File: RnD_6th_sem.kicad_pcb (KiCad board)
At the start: 2 copper layers, 62 x 69.1 mm, 79 parts, among them IC1 2EDF7275KXUMA1, J1 HVDC, J10 MMCX-J-P-H-ST-TH1, J2 PWM, J3 HVDC, J4 Conn_02x05_Odd_Even, J5 5V, J6 5V, J7 GND, J8 GND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

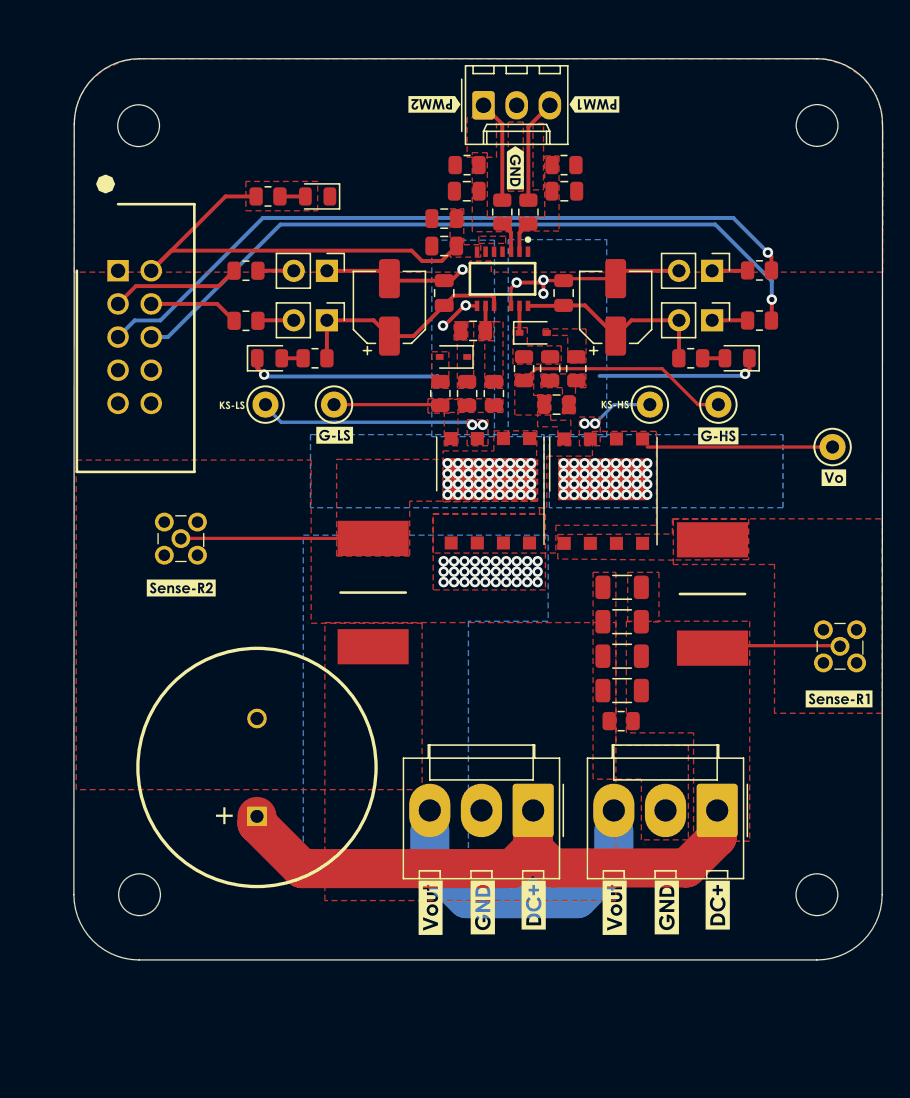
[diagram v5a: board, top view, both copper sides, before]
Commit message: updated the layout of FB and caps
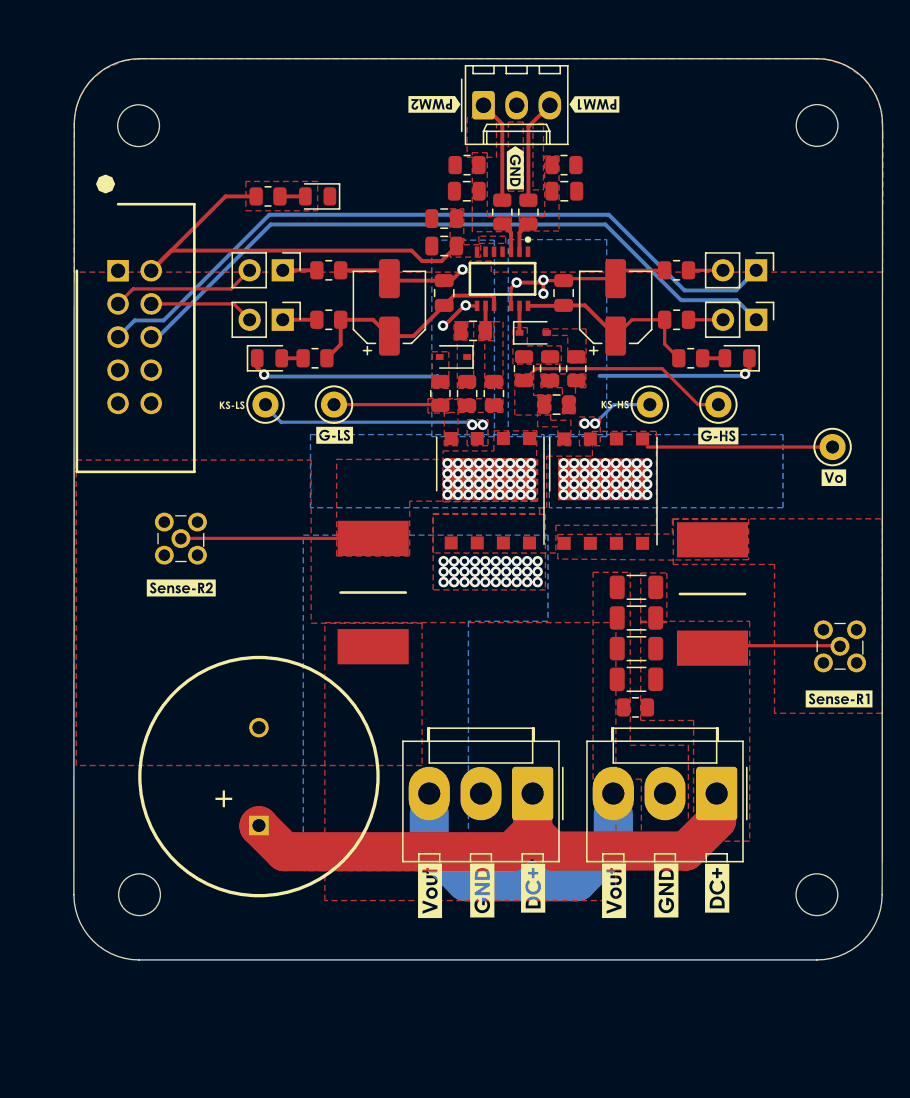
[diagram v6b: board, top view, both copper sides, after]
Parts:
- added kibuzzard-63FF27E9: G***, kibuzzard-63FF27E9, B.Cu at (153.1, 96.2)
- added kibuzzard-63FF2952: G***, kibuzzard-63FF2952, B.Cu at (124.6, 77.9)
- moved FB4 6.35 mm to (152.0, 67.8), turned to 0 degrees
- moved FB1 6.35 mm to (152.0, 64.0)
- moved FB3 6.34 mm to (125.4, 67.8), turned to 180 degrees
- moved FB2 6.34 mm to (125.4, 64.0)
- moved J6 3.38 mm to (121.9, 67.8)
- moved J7 3.38 mm to (121.9, 64.0)
- moved J5 3.38 mm to (158.1, 67.8)
- moved J8 3.38 mm to (158.1, 64.0)
- moved R8 1.52 mm to (148.9, 97.5)
- moved C7 1.40 mm to (149.0, 95.3)
- moved kibuzzard-63EE9044 1.30 mm to (155.1, 111.3)
- moved kibuzzard-63EE9044 1.30 mm to (141.0, 111.3)
- moved kibuzzard-63EE9059 1.30 mm to (137.1, 111.5)
- moved kibuzzard-63EE9091 1.30 mm to (133.1, 111.5)
- moved J1 1.30 mm to (155.1, 104.1)
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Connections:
- FB1 pad 1: GND1 -> gnd-1
- FB2 pad 2: GND2 -> gnd-2
- FB3 pad 1: Net-(FB3-Pad1) -> LED2
- FB3 pad 2: VCCB -> Net-(FB3-Pad2)
- FB4 pad 1: Net-(FB4-Pad1) -> LED1
- FB4 pad 2: VCCA -> Net-(FB4-Pad2)
- J4 pad 3: Net-(FB2-Pad1) -> GND2
- J4 pad 4: Net-(FB3-Pad1) -> VCCB
- J4 pad 5: Net-(FB1-Pad2) -> GND1
- J4 pad 6: Net-(FB4-Pad1) -> VCCA
- J5 pad 2: LED1 -> Net-(FB4-Pad2)
- J6 pad 1: LED2 -> Net-(FB3-Pad2)
- J7 pad 1: gnd-2 -> Net-(FB2-Pad1)
- J8 pad 2: gnd-1 -> Net-(FB1-Pad2)
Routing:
- net Net-(FB4-Pad1): track 56.0 -> 0.00 mm, vias 1 -> 0
- net Net-(FB1-Pad2): track 56.1 -> 2.64 mm, vias 1 -> 0
- net GND1: track 2.73 -> 55.8 mm
- net VCCA: track 2.72 -> 53.0 mm
- net GND2: track 2.75 -> 11.1 mm
- net Net-(FB2-Pad1): track 9.94 -> 2.61 mm
- net Net-(FB3-Pad1): track 6.89 -> 0.00 mm
- net VCCB: track 2.76 -> 8.04 mm
- net Net-(FB4-Pad2): track 0.00 -> 2.65 mm
- net Net-(FB3-Pad2): track 0.00 -> 2.61 mm
- net HVDC+: track 57.2 -> 55.9 mm
- net gnd-1: track 33.4 -> 32.3 mm
- net gnd-2: track 45.6 -> 44.6 mm
- net LED1: track 16.0 -> 15.4 mm
- net LED2: track 18.2 -> 17.6 mm

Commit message: Final design
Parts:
- added kibuzzard-63FF2B27: G***, kibuzzard-63FF2B27, F.Cu at (117.4, 106.5)
- J4: value Conn_02x05_Odd_Even -> Conn_02x03_Odd_Even; footprint 61201021621:SHDR10W64P254_2X5_2036X885X925P -> Connector_PinSocket_2.54mm:PinSocket_2x03_P2.54mm_Horizontal
- moved J4 5.66 mm to (114.9, 63.5), turned to 0 degrees
- moved kibuzzard-63EDDA14 3.30 mm to (107.7, 60.6)
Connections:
- J4 pad 1: GND -> +3.3V
- J4 pad 2: +3.3V -> GND
- J4 pad 3: GND2 -> VCCB
- J4 pad 4: VCCB -> GND2
- J4 pad 5: GND1 -> VCCA
- J4 pad 6: VCCA -> GND1
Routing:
- net Net-(J1-Pin_3): track 35.4 -> 50.7 mm
- net +3.3V: track 35.2 -> 30.2 mm
- net GND2: track 11.1 -> 7.84 mm
- net VCCB: track 8.04 -> 5.14 mm
- net GND1: track 55.8 -> 53.5 mm
- net VCCA: track 53.0 -> 51.8 mm
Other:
- board text removed: "+"

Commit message: final design mar-08
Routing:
- net gnd-1: track 32.1 -> 47.9 mm
- net gnd-2: track 44.6 -> 55.4 mm
- net Net-(J1-Pin_3): track 50.7 -> 44.3 mm
